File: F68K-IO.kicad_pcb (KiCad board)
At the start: 2 copper layers, 125.1 x 95.9 mm, 74 parts, among them J1 JOYPAD A, J10 MIDI IN, J11 MIDI OUT, J12 HDMI, J13 HDMI (Alt), J14 MIDI IN (Alt), J15 MIDI OUT (Alt), J16 FDD EXT PWR IN, J17 FDD PWR OUT, J2 AUDIO OUT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

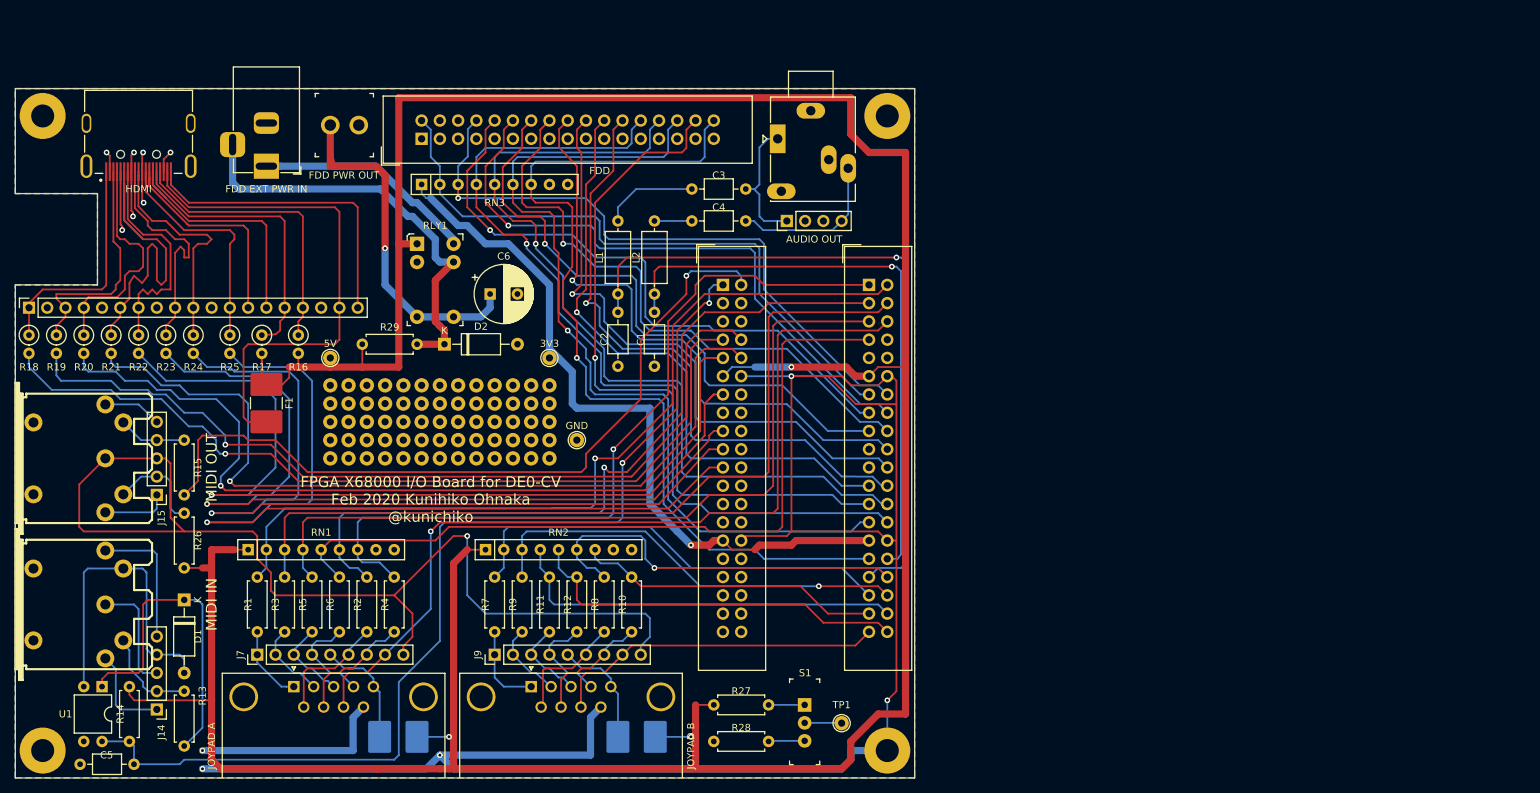
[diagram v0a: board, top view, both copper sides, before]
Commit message: Fix JOYPAD signal pull-up voltage from 5V to 3.3V.
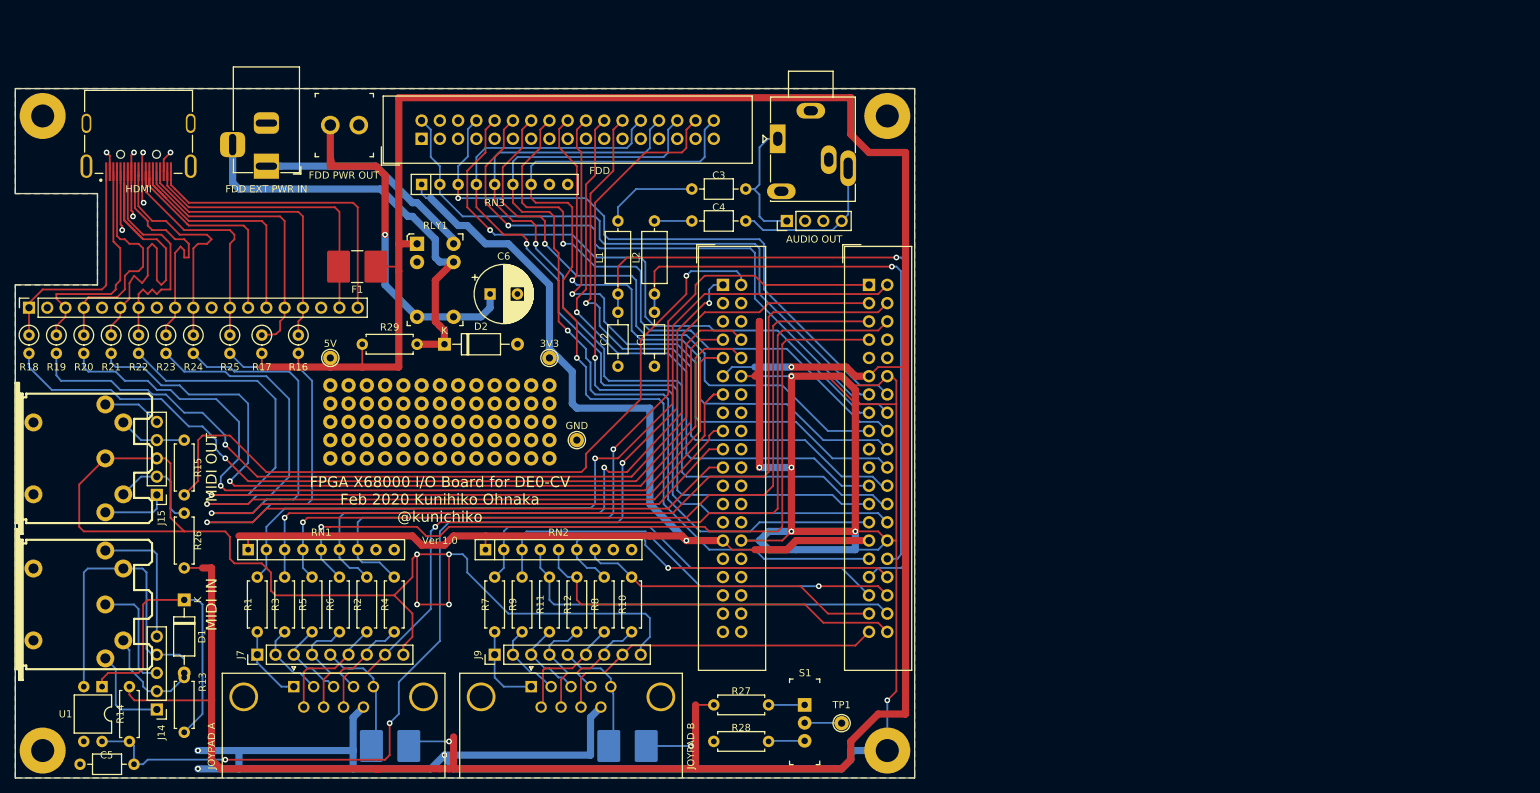
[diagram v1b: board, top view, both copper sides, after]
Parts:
- J2: footprint Connector_Audio:Jack_3.5mm_Ledino_KB3SPRS_Horizontal -> F68K-IO:Jack_3.5mm_Ledino_KB3SPRS_Horizontal
- moved F1 22.8 mm to (135.8, 68.6), turned to 180 degrees
- moved R13 1.91 mm to (111.8, 125.7)
- moved F3 1.80 mm to (173.4, 135.3)
- moved F2 1.71 mm to (140.4, 135.3)
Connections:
- RN1 pad 1: +5V -> +3V3
- RN2 pad 1: +5V -> +3V3
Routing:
- net GND: track 465.3 -> 608.6 mm, vias 14 -> 21
- net +3V3: track 108.4 -> 175.2 mm
- net +5V: track 466.9 -> 426.1 mm
- net /HDMI_18_5V: track 72.5 -> 40.7 mm
- net /JOYAPD-A-DSUB_4: track 108.6 -> 111.5 mm, vias 0 -> 1
- net Net-(D1-Pad2): track 43.4 -> 41.5 mm
- net Net-(D1-Pad1): track 45.8 -> 43.9 mm
- net Net-(F2-Pad2): track 16.8 -> 17.9 mm
- net Net-(C5-Pad1): track 143.9 -> 142.8 mm, vias 2 -> 4
- net /JOYAPD-B-DSUB_6: track 54.5 -> 53.4 mm
- net Net-(J10-Pad4): track 13.5 -> 14.3 mm
- net /JOYAPD-A-DSUB_3: vias 0 -> 1
- net /JOYAPD-A-DSUB_2: vias 0 -> 1
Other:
- board text added: "Ver 1.0"

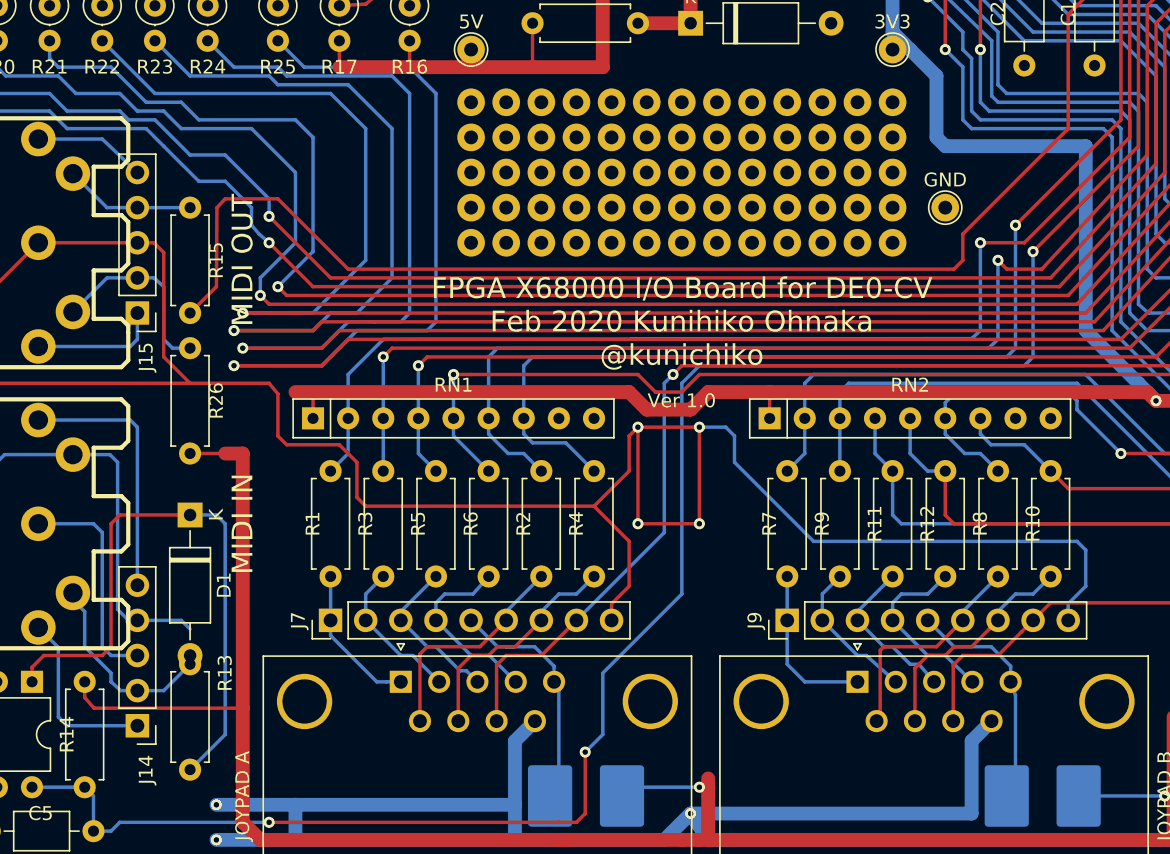
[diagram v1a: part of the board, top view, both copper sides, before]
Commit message: Fix some connection failures.
* Change MIDI IN signal pull-up voltage from 5V to 3.3V
* Flip HDMI D0+ and D0-
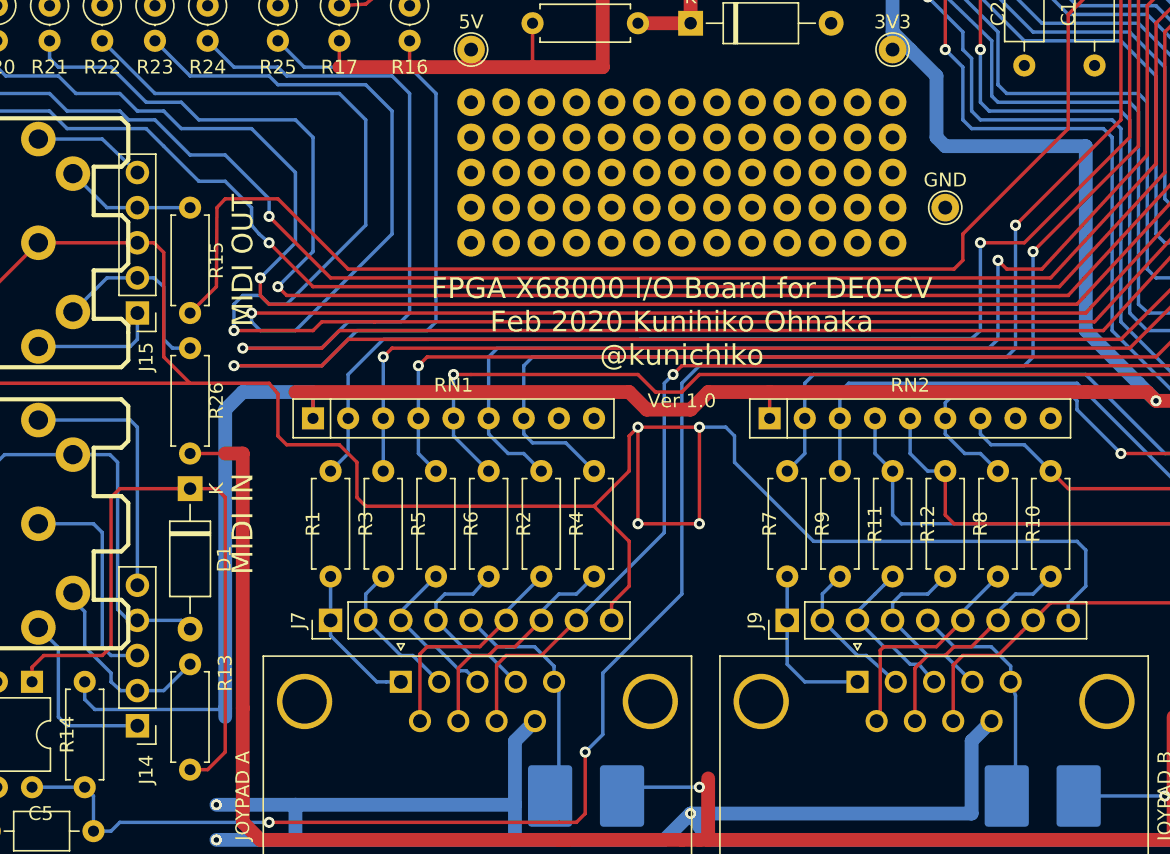
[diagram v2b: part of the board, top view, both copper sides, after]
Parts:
- C3, C4: value C -> 0.1μ
- moved D1 1.91 mm to (111.8, 113.0)
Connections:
- J5 pad 13: /HDMI_D0+ -> /HDMI_D0-
- J5 pad 17: /HDMI_D0- -> /HDMI_D0+
- R14 pad 1: +5V -> +3V3
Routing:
- net +3V3: track 175.2 -> 218.0 mm
- net +5V: track 426.1 -> 413.2 mm
- net Net-(D1-Pad1): track 43.9 -> 48.4 mm
- net /HDMI_D0+: track 122.3 -> 119.9 mm
- net /HDMI_D0-: track 120.1 -> 122.1 mm

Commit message: Work in progress
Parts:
- removed 3V3, 5V, GND: TestPoint_THTPad_D2.0mm_Drill1.0mm, TestPoint:TestPoint_THTPad_D2.0mm_Drill1.0mm
- removed J13: HDMI (Alt), Connector_PinSocket_2.54mm:PinSocket_1x19_P2.54mm_Vertical
- removed J7, J9: Conn_01x09_Male, Connector_PinHeader_2.54mm:PinHeader_1x09_P2.54mm_Vertical
- removed REF**: UniversalPattern_5x13, F68K-IO:UniversalPattern_5x13
- added C7: 1F 5.5V, F68K-IO:SuperCapacitor_SE-SR5-D105VYV, F.Cu at (264.3, 63.9)
- added D3: D, Diode_THT:D_A-405_P10.16mm_Horizontal, F.Cu at (276.5, 62.1)
- added R30: 220, Resistor_THT:R_Axial_DIN0207_L6.3mm_D2.5mm_P7.62mm_Horizontal, F.Cu at (266.1, 78.5)
- added R31: 1.8k, Resistor_THT:R_Axial_DIN0207_L6.3mm_D2.5mm_P7.62mm_Horizontal, F.Cu at (289.9, 66.0)
- added R32: 1.8k, Resistor_THT:R_Axial_DIN0207_L6.3mm_D2.5mm_P7.62mm_Horizontal, F.Cu at (276.8, 78.5)
- added S2: EG1218, digikey-footprints:Switch_Slide_11.6x4mm_EG1218, F.Cu at (267.3, 99.1)
- added TP2: TestPoint, TestPoint:TestPoint_THTPad_D2.0mm_Drill1.0mm, F.Cu at (288.5, 70.3)
- added TP3: TestPoint, TestPoint:TestPoint_THTPad_D2.0mm_Drill1.0mm, F.Cu at (292.5, 70.1)
- added U2: AE-RX-8025NB, F68K-IO:AE-RX-8025NB, F.Cu at (258.6, 76.6)
- added U3: RX-8025SA, SMD_Packages:SOIC-14_N, F.Cu at (270.1, 72.1)
- C1, C2: value 10μ -> 1000pF; footprint Capacitor_THT:C_Axial_L3.8mm_D2.6mm_P7.50mm_Horizontal -> F68K-IO:C_Axial_L3.8mm_D2.6mm_P5.00mm_Horizontal
- C3: value 0.1μ -> 10μ
- C4: value 0.1μ -> 0.33μ
- C6: value 100u -> 220u
- J5, J6: footprint Connector_IDC:IDC-Header_2x20_P2.54mm_Vertical -> F68K-IO:IDC-Header_2x20_P2.54mm_Vertical_OvalPad
- R1, R10, R11, R12, R2, R3, R4, R5, R6, R7, R8, R9: footprint Resistor_THT:R_Axial_DIN0207_L6.3mm_D2.5mm_P7.62mm_Horizontal -> Resistor_THT:R_Axial_DIN0207_L6.3mm_D2.5mm_P2.54mm_Vertical
- R27, R28: value 4.7k -> 220
- R29: value 47 -> 220
- moved R27 124.4 mm to (289.9, 62.0)
- moved R28 108.6 mm to (277.4, 66.2), turned to 0 degrees
- moved C2 105.4 mm to (277.4, 70.3), turned to 0 degrees
- moved C1 89.2 mm to (266.1, 82.5), turned to 0 degrees
- moved R17 87.6 mm to (198.8, 34.9)
- moved R16 85.9 mm to (201.9, 34.9)
- moved R18 79.8 mm to (168.3, 61.6)
- moved R19 79.2 mm to (171.4, 61.6)
- moved R20 78.6 mm to (174.6, 61.6)
- moved R21 78.0 mm to (177.8, 61.6)
- moved R22 77.3 mm to (181.0, 61.6)
- moved R23 76.7 mm to (184.2, 61.6)
- moved J12 76.2 mm to (181.6, 54.6)
- moved R24 76.1 mm to (187.3, 61.6)
- moved R25 74.2 mm to (190.5, 61.6)
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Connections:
- net Net-(C5-Pad1) renamed /MIDI_IN
- net Net-(J11-Pad5) renamed /MIDI_OUT
- C1 pad 1: /AUDIO_R -> Net-(C1-Pad1)
- C2 pad 1: /AUDIO_L -> Net-(C2-Pad1)
- C3 pad 1: Net-(C3-Pad1) -> Net-(C1-Pad1)
- C4 pad 1: Net-(C4-Pad1) -> Net-(C2-Pad1)
- J2 pad R: Net-(C4-Pad1) -> Net-(C2-Pad1)
- J2 pad T: Net-(C3-Pad1) -> Net-(C1-Pad1)
- J8 pad 1: Net-(C3-Pad1) -> Net-(C1-Pad1)
- J8 pad 4: Net-(C4-Pad1) -> Net-(C2-Pad1)
- R27 pad 2: Net-(R27-Pad2) -> Net-(D2-Pad1)
- R28 pad 1: Net-(R28-Pad1) -> +5V
- R28 pad 2: GND -> Net-(D2-Pad1)
- RLY1 pad 1: +5V -> Net-(C6-Pad1)
- RLY1 pad 10: Net-(J16-Pad1) -> Net-(C6-Pad1)
- RLY1 pad 2: GND -> Net-(D2-Pad1)
- RLY1 pad 5: Net-(C6-Pad1) -> Net-(J16-Pad1)
- RLY1 pad 6: Net-(C6-Pad1) -> +5V
- RLY1 pad 9: Net-(D2-Pad1) -> GND
- S1 pad 1: Net-(R27-Pad2) -> Net-(S1-Pad1)
- S1 pad 3: Net-(R28-Pad1) -> GND
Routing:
- net /HDMI_CK-: track 120.3 -> 1.91 mm, vias 1 -> 0
- net /HDMI_CK+: track 120.2 -> 1.91 mm, vias 1 -> 0
- net /HDMI_D0+: track 119.9 -> 2.80 mm, vias 1 -> 0
- net /HDMI_D0-: track 122.1 -> 8.41 mm, vias 1 -> 0
- net /HDMI_D1+: track 120.1 -> 13.0 mm, vias 1 -> 0
- net /HDMI_D2+: track 120.0 -> 15.1 mm, vias 1 -> 0
- net /HDMI_D1-: track 120.1 -> 16.9 mm, vias 1 -> 0
- net /HDMI_D2-: track 120.0 -> 19.1 mm, vias 1 -> 0
- net /HDMI_6_D1-: track 51.7 -> 0.00 mm
- net /HDMI_16_SDA: track 40.2 -> 0.00 mm
- net /HDMI_15_SCL: track 39.9 -> 0.00 mm
- net /HDMI_14_UTILITY: track 34.3 -> 0.00 mm
- net /HDMI_12_CK-: track 34.0 -> 0.00 mm
- net Net-(C6-Pad1): track 56.9 -> 90.3 mm
- net Net-(J16-Pad1): track 33.4 -> 0.00 mm
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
